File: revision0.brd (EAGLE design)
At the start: 80 x 100 mm, 93 parts, among them IC1 MSP430FR698X(1)80-PIN_PN, IC3 FT232RL

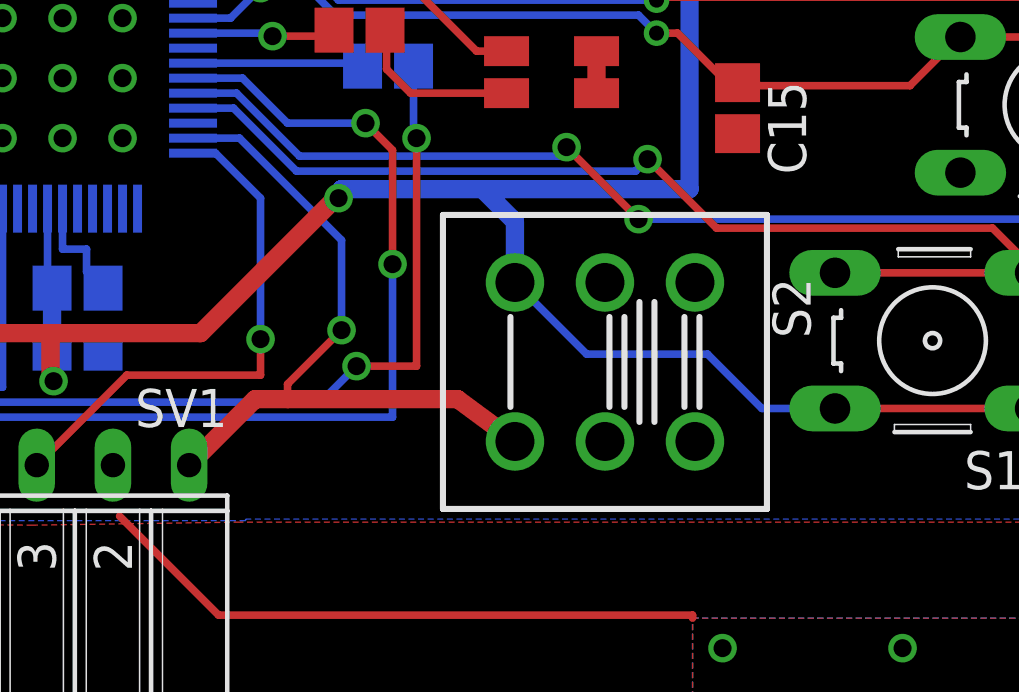
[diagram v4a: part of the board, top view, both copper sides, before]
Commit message: Fix CANAL sliding switch
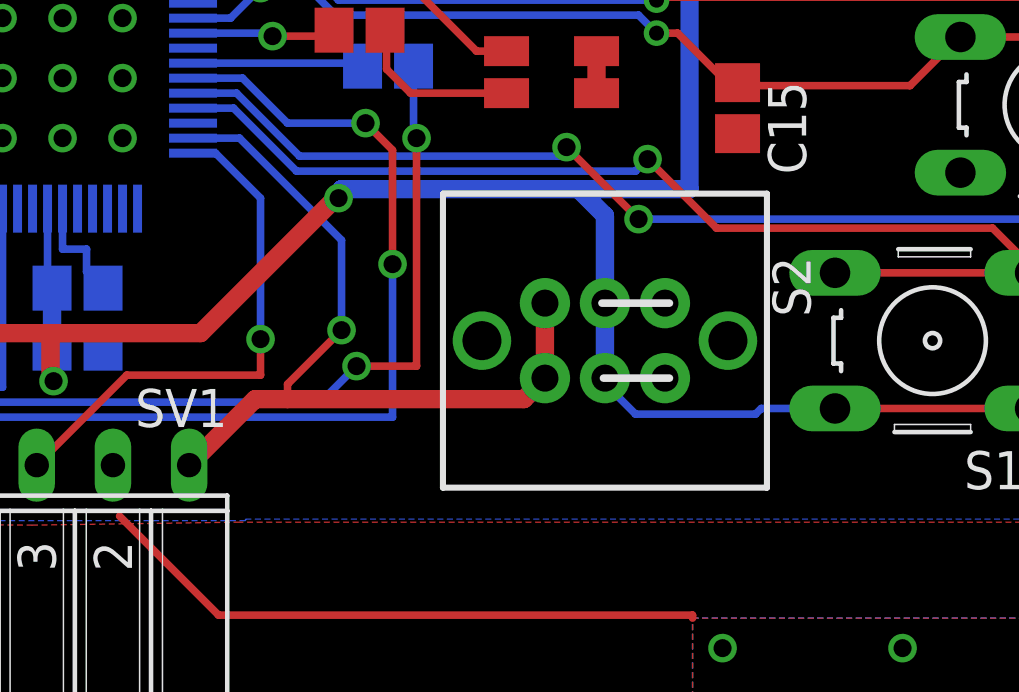
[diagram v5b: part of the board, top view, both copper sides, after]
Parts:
- moved S2 0.71 mm to (33.1, 36.2)
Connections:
- net GND: now also S2.1.1, S2.1.2
- net MB_PWR_GPS_SENSE: now also S2.3.2
- net VCC: now also S2.2.1, S2.2.2; no longer S2.3.2
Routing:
- net MB_PWR_GPS_SENSE: track 24.6 -> 28.0 mm
- net VCC: track 202.9 -> 201.9 mm
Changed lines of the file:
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@@
 <attribute name="OC_FARNELL" value="176432" x="44" y="36.25" size="1.778" layer="27" rot="R180" display="off"/>
 </element>
-<element name="S2" library="tagps" package="2P2T" value="2P2T" x="33.08" y="35.54" rot="R180"/>
+<element name="S2" library="tagps" package="2P2T" value="2P2T" x="33.08" y="36.25" rot="R180"/>
 <element name="S3" library="tagps" package="B3F-10XX" value="" x="55" y="36.25" rot="R180">
 <attribute name="OC_NEWARK" value="36M3542" x="55" y="36.25" size="1.778" layer="27" rot="R180" display="off"/>
@@
 <contactref element="C2" pad="2"/>
 <contactref element="R1" pad="1"/>
-<contactref element="S2" pad="3.2"/>
 <contactref element="S3" pad="2"/>
 <contactref element="S3" pad="1"/>
@@
 <wire x1="42.35" y1="52.35" x2="42.35" y2="53" width="0.6096" layer="1"/>
 <wire x1="4.3" y1="36.5" x2="6.2" y2="36.5" width="0.6096" layer="16"/>
-<wire x1="24.3" y1="41.3" x2="29" y2="41.3" width="0.6096" layer="16"/>
-<wire x1="29" y1="41.3" x2="35.9" y2="41.3" width="0.6096" layer="16"/>
+<wire x1="24.3" y1="41.3" x2="32.2" y2="41.3" width="0.6096" layer="16"/>
+<wire x1="32.2" y1="41.3" x2="35.9" y2="41.3" width="0.6096" layer="16"/>
 <wire x1="35.9" y1="41.3" x2="35.9" y2="49.9" width="0.6096" layer="16"/>
 <wire x1="51.45" y1="59.05" x2="51.5" y2="61" width="0.254" layer="1"/>
@@
 <wire x1="51.7488" y1="33.9894" x2="58.2512" y2="33.9894" width="0.254" layer="1"/>
 <wire x1="40.7488" y1="33.9894" x2="47.2512" y2="33.9894" width="0.254" layer="1"/>
-<wire x1="30.08" y1="38.19" x2="30.08" y2="40.22" width="0.6096" layer="16"/>
-<wire x1="30.08" y1="40.22" x2="29" y2="41.3" width="0.6096" layer="16"/>
-<wire x1="40.7488" y1="33.9894" x2="38.3106" y2="33.9894" width="0.254" layer="16"/>
-<wire x1="38.3106" y1="33.9894" x2="36.5" y2="35.8" width="0.254" layer="16"/>
-<wire x1="36.5" y1="35.8" x2="32.47" y2="35.8" width="0.254" layer="16"/>
-<wire x1="32.47" y1="35.8" x2="30.08" y2="38.19" width="0.254" layer="16"/>
+<wire x1="40.7488" y1="33.9894" x2="38.2894" y2="33.9894" width="0.254" layer="16"/>
 <wire x1="51.7488" y1="33.9894" x2="47.2512" y2="33.9894" width="0.254" layer="1"/>
 <wire x1="24.2" y1="41" x2="24.1" y2="41" width="0.6096" layer="1"/>
@@
 <wire x1="14.7" y1="34.9" x2="14.6" y2="35" width="0.6096" layer="1"/>
 <wire x1="14.6" y1="35" x2="14.6" y2="36.5" width="0.6096" layer="1"/>
+<contactref element="S2" pad="2.1"/>
+<contactref element="S2" pad="2.2"/>
+<wire x1="33.08" y1="37.5" x2="33.08" y2="35" width="0.6096" layer="16"/>
+<wire x1="33.08" y1="37.5" x2="33.08" y2="40.42" width="0.6096" layer="16"/>
+<wire x1="33.08" y1="40.42" x2="32.2" y2="41.3" width="0.6096" layer="16"/>
+<wire x1="34.1" y1="33.8" x2="33.2" y2="34.7" width="0.254" layer="16"/>
+<wire x1="38.1" y1="33.8" x2="34.1" y2="33.8" width="0.254" layer="16"/>
+<wire x1="38.2894" y1="33.9894" x2="38.1" y2="33.8" width="0.254" layer="16"/>
+<wire x1="33.2" y1="34.7" x2="33.08" y2="35" width="0.254" layer="16"/>
 </signal>
 <signal name="GND">
@@
 <wire x1="36" y1="27.1" x2="20.2" y2="27.1" width="0.254" layer="1"/>
 <wire x1="36" y1="27.1" x2="36" y2="27" width="0.254" layer="1"/>
+<contactref element="S2" pad="1.2"/>
+<contactref element="S2" pad="1.1"/>
 </signal>
 <signal name="GPS-WAKEUP">
@@
 </signal>
 <signal name="MB_PWR_GPS_SENSE">
-<contactref element="S2" pad="3.1"/>
 <contactref element="IC1" pad="39"/>
-<wire x1="30.08" y1="32.89" x2="28.17" y2="34.3" width="0.6096" layer="1"/>
-<wire x1="28.17" y1="34.3" x2="22.5" y2="34.3" width="0.6096" layer="1"/>
+<wire x1="30.38" y1="34.3" x2="22.5" y2="34.3" width="0.6096" layer="1"/>
 <wire x1="19.35" y1="43" x2="20.9" y2="43" width="0.254" layer="16"/>
 <wire x1="20.9" y1="43" x2="24.3" y2="39.6" width="0.254" layer="16"/>
@@
 <wire x1="24.3" y1="36.6" x2="22.5" y2="34.8" width="0.254" layer="1"/>
 <wire x1="22.5" y1="34.8" x2="22.5" y2="34.3" width="0.254" layer="1"/>
+<wire x1="21.42" y1="34.3" x2="22.5" y2="34.3" width="0.6096" layer="1"/>
+<contactref element="S2" pad="3.2"/>
+<contactref element="S2" pad="3.1"/>
 <contactref element="SV1" pad="1"/>
-<wire x1="19.22" y1="32.1" x2="21.42" y2="34.3" width="0.6096" layer="1"/>
-<wire x1="21.42" y1="34.3" x2="22.5" y2="34.3" width="0.6096" layer="1"/>
+<wire x1="31.08" y1="35" x2="31.08" y2="37.5" width="0.6096" layer="1"/>
+<wire x1="21.42" y1="34.3" x2="19.22" y2="32.1" width="0.6096" layer="1"/>
+<wire x1="30.38" y1="34.3" x2="31.08" y2="35" width="0.6096" layer="1"/>
 </signal>
 <signal name="MB-GPS-WAKEUP">

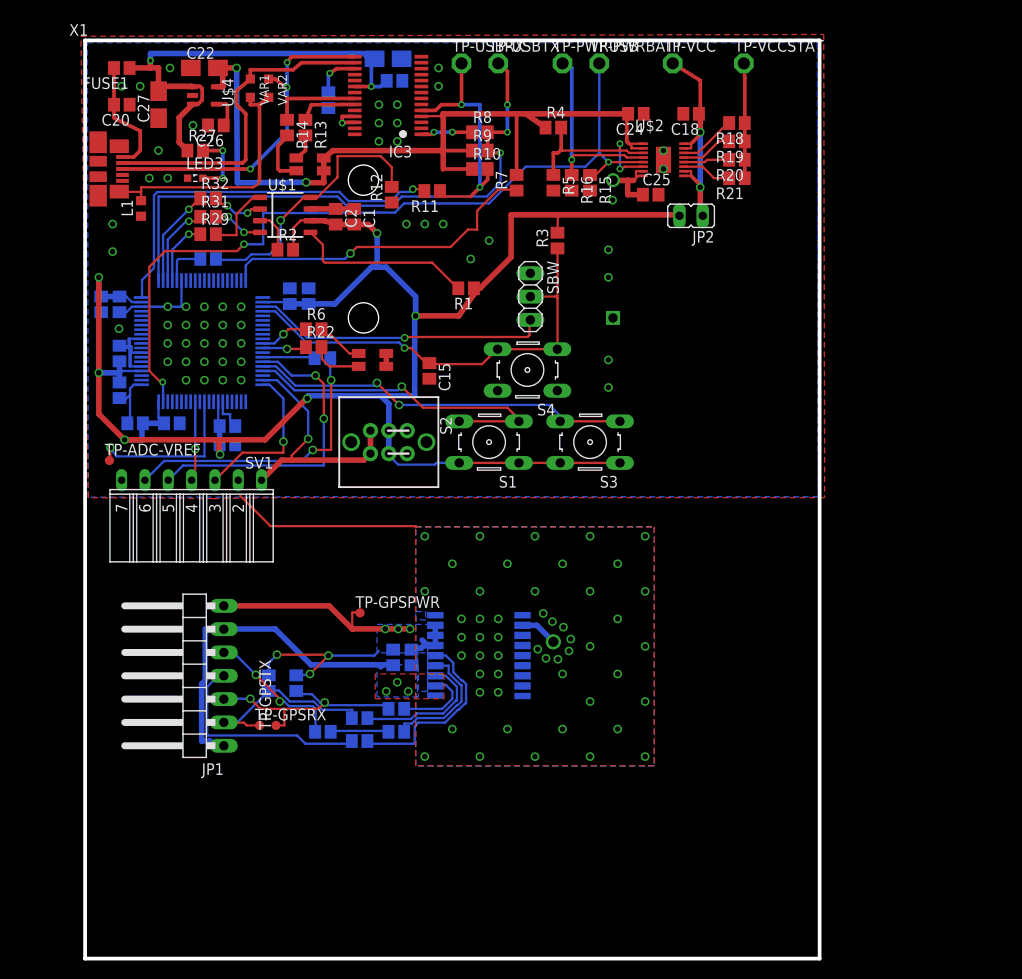
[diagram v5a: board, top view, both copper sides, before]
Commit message: Add MWSL1251 antenna to taGPS design
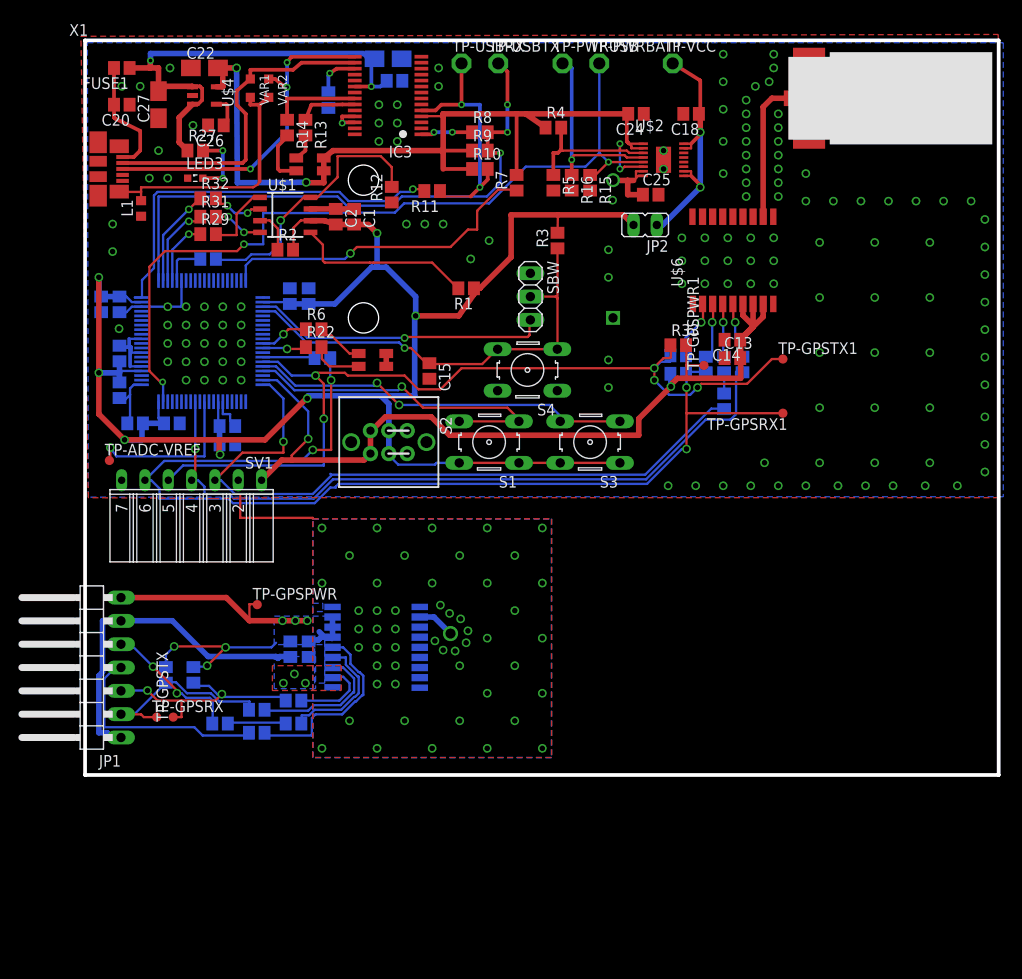
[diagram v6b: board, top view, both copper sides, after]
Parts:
- removed R18, R19, R20, R21: 470k, tagps:R0805
- removed TP-VCCSTAT: TPSQPAD1-13, tagps:P1-13
- added C13: 100n, tagps:C0805
- added C14: 1u, tagps:C0805
- added FB4, FB5, FB6, R34, R35: 0, tagps:R0805
- added R17, R33: 100k, tagps:R0805
- added TP-GPSPWR1, TP-GPSRX1, TP-GPSTX1: TPSQTP10R, tagps:TP10R
- added U$5: MWSL1251, tagps:MWSL1251
- added U$6: MAX-8C-0, tagps:MAX-8
- moved TP1 11.2 mm to (39.8, 15.4)
- moved U$3 11.2 mm to (36.5, 8.85)
- moved JP1 11.2 mm to (0.10, 11.7)
- moved TP-GPSTX 11.2 mm to (9.60, 6.30)
- moved FB1 11.2 mm to (18.7, 7.10)
- moved FB2 11.2 mm to (22.7, 8.10)
- moved FB3 11.2 mm to (22.7, 5.60)
- moved R24 11.2 mm to (8.80, 10.9)
- moved R25 11.2 mm to (11.8, 10.9)
- moved R26 11.2 mm to (18.7, 4.60)
- moved R28 11.2 mm to (14.7, 5.60)
- moved TP-GPSPWR 11.2 mm to (18.8, 18.6)
- moved TP-GPSRX 11.2 mm to (7.80, 6.30)
- moved C16 11.2 mm to (24.4, 13.7)
- moved C17 11.2 mm to (22.4, 13.7)
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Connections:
- removed net MB_PWR_GPS_SENSE: IC1.39, S2.3.1, S2.3.2, SV1.1
- removed net N$28: R20.2, U$2.12
- removed net N$29: R19.2, U$2.13
- removed net N$30: R18.2, U$2.14
- removed net N$31: R18.1, R19.1, R20.1, R21.1, TP-VCCSTAT.TP
- new net MB-PWR_GPS_SENSE: C13.2, C14.1, IC1.39, R17.2, R33.2, S2.3.1, S2.3.2, SV1.1, TP-GPSPWR1.TP, U$6.6, U$6.7, U$6.8
- new net N$46: R34.2, U$6.5
- new net N$47: FB6.2, R35.2
- new net N$48: FB4.1, U$6.3
- new net N$49: FB5.1, U$6.2
- new net N$50: FB6.1, U$6.4
- net GND: now also C13.1, C14.2, U$5.P$1, U$5.P$3, U$6.1, U$6.10, U$6.12
- net MB-GPS-RX: now also FB4.2, R17.1, TP-GPSRX1.TP
- net MB-GPS-TIMEPULSE: now also R35.1
- net MB-GPS-TX: now also FB5.2, R33.1, TP-GPSTX1.TP
- net MB-GPS-WAKEUP: now also R34.1
- net N$27: now also U$5.P$2, U$6.11; no longer R21.2, U$2.11
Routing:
- net MB-PWR_GPS_SENSE: track 0.00 -> 99.1 mm, vias 0 -> 2
- net MB-GPS-RX: track 31.7 -> 116.0 mm, vias 2 -> 4
- net MB-GPS-WAKEUP: track 8.72 -> 78.5 mm
- net MB-GPS-TX: track 34.1 -> 97.0 mm, vias 2 -> 5
- net MB-GPS-TIMEPULSE: track 17.5 -> 77.7 mm
- net MB_PWR_GPS_SENSE: track 28.0 -> 0.00 mm, vias 1 -> 0
- net N$31: track 12.5 -> 0.00 mm
- net N$27: track 5.47 -> 16.3 mm
- net GND: track 96.9 -> 86.8 mm, vias 109 -> 193
- net N$48: track 0.00 -> 6.49 mm, vias 0 -> 1
- net N$49: track 0.00 -> 6.44 mm, vias 0 -> 1
- net N$46: track 0.00 -> 6.33 mm, vias 0 -> 1
- net N$30: track 6.30 -> 0.00 mm
- net N$50: track 0.00 -> 5.89 mm, vias 0 -> 1
- net N$29: track 5.67 -> 0.00 mm
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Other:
- board size 80 x 100 mm -> 99.5 x 80 mm

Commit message: Small board tuning
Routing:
- net GND: vias 193 -> 194
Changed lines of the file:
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@@
 <setting verticaltext="up"/>
 </settings>
-<grid distance="2" unitdist="mm" unit="mm" style="lines" multiple="1" display="yes" altdistance="0.025" altunitdist="inch" altunit="inch"/>
+<grid distance="0.05" unitdist="mm" unit="mm" style="lines" multiple="1" display="yes" altdistance="0.025" altunitdist="inch" altunit="inch"/>
 <layers>
 <layer number="1" name="Top" color="4" fill="1" visible="yes" active="yes"/>
@@
 <text x="0.85" y="37.7" size="1.016" layer="100" rot="R270">ADC-VREF</text>
 <text x="49.7" y="74.9" size="1.016" layer="100">USB-PWR-BATT</text>
-<dimension x1="0" y1="0" x2="80" y2="0" x3="40" y3="-6.4" textsize="1.778" layer="1"/>
 <text x="0.9" y="11.1" size="1.016" layer="100">TIMEPULSE</text>
 <text x="77.2" y="46" size="1.016" layer="100" rot="R270">RX-GPS-TX</text>
+<dimension x1="98.25" y1="63.7" x2="98.25" y2="68.7" x3="103.104259375" y3="66.2" textsize="1.778" layer="1"/>
+<dimension x1="0" y1="0" x2="99.5" y2="0" x3="49.75" y3="-5.1" textsize="1.778" layer="1"/>
+<dimension x1="0" y1="80" x2="0" y2="0" x3="-10.6" y3="40" textsize="1.778" layer="1"/>
 </plain>
 <attributes>
@@
 <via x="72.5" y="31.5" extent="1-16" drill="0.6"/>
 <via x="74" y="34" extent="1-16" drill="0.6"/>
+<via x="72.35" y="78.5" extent="1-16" drill="0.6"/>
 </signal>
 <signal name="GPS-WAKEUP">

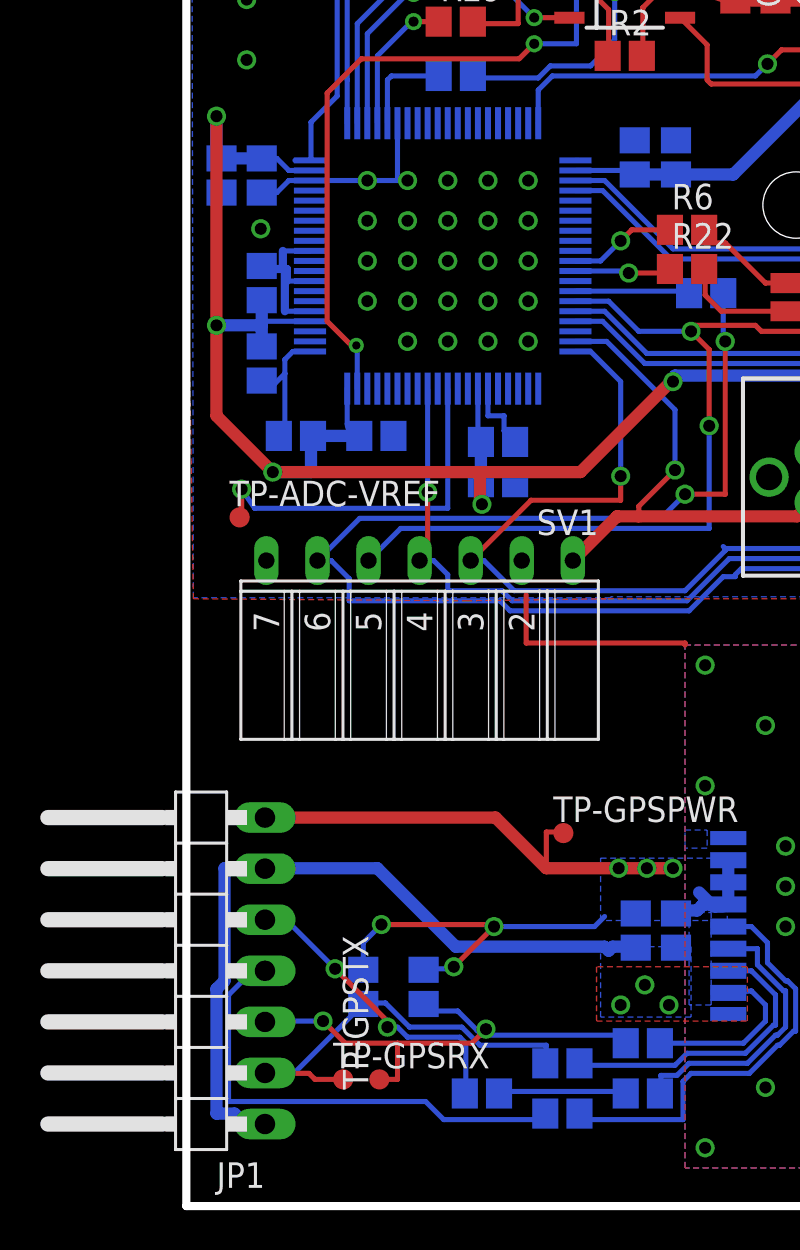
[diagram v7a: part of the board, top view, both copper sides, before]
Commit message: Rotate connector of patch antenna
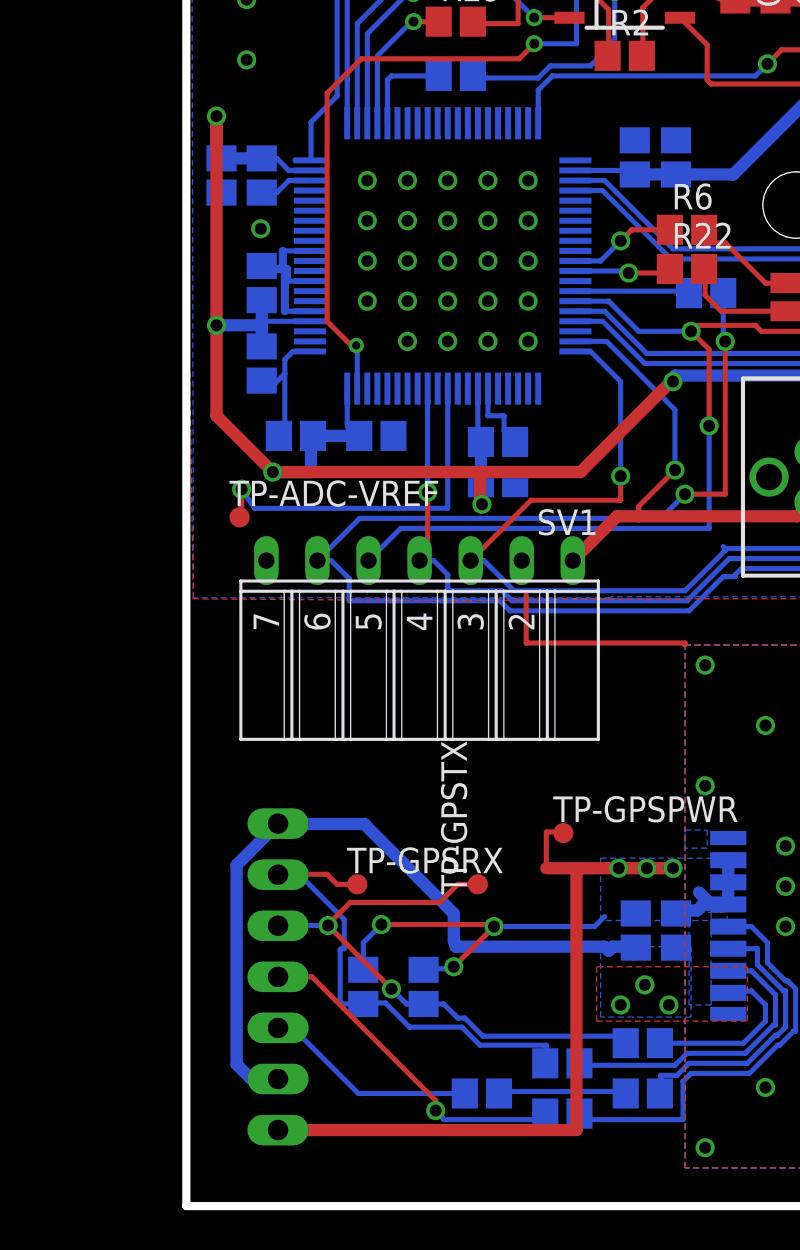
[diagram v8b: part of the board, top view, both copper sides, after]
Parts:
- moved TP-GPSTX 10.9 mm to (14.5, 16.0)
- moved TP-GPSRX 9.73 mm to (8.50, 16.0)
- moved JP1 0.72 mm to (0.75, 11.4), flipped to the bottom, turned to 270 degrees
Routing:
- net PWR_GPS_SENSE: track 46.4 -> 59.2 mm
- net GND: track 86.8 -> 78.9 mm
- net GPS-WAKEUP: track 24.1 -> 17.0 mm, vias 0 -> 1
- net GPS-TIMEPULSE: track 15.3 -> 10.6 mm, vias 2 -> 0
- net GPS-RX: track 21.3 -> 24.9 mm
- net GPS-TX: track 26.1 -> 28.2 mm
